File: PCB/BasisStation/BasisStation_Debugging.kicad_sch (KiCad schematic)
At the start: 14 parts, among them J1 USB_B_Micro, U1 D3V3XA4B10LP, U2 TLV75801PDRV, U3 CP2102N-Axx-xQFN28

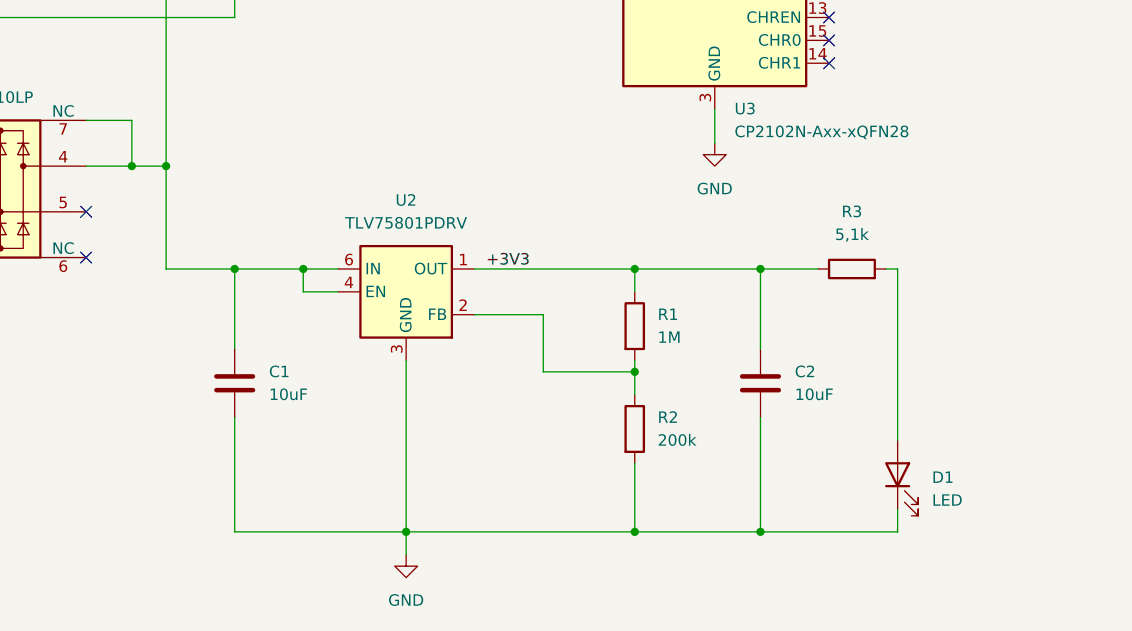
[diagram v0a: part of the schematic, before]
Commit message: Entfernung der LED im Debugging Layout
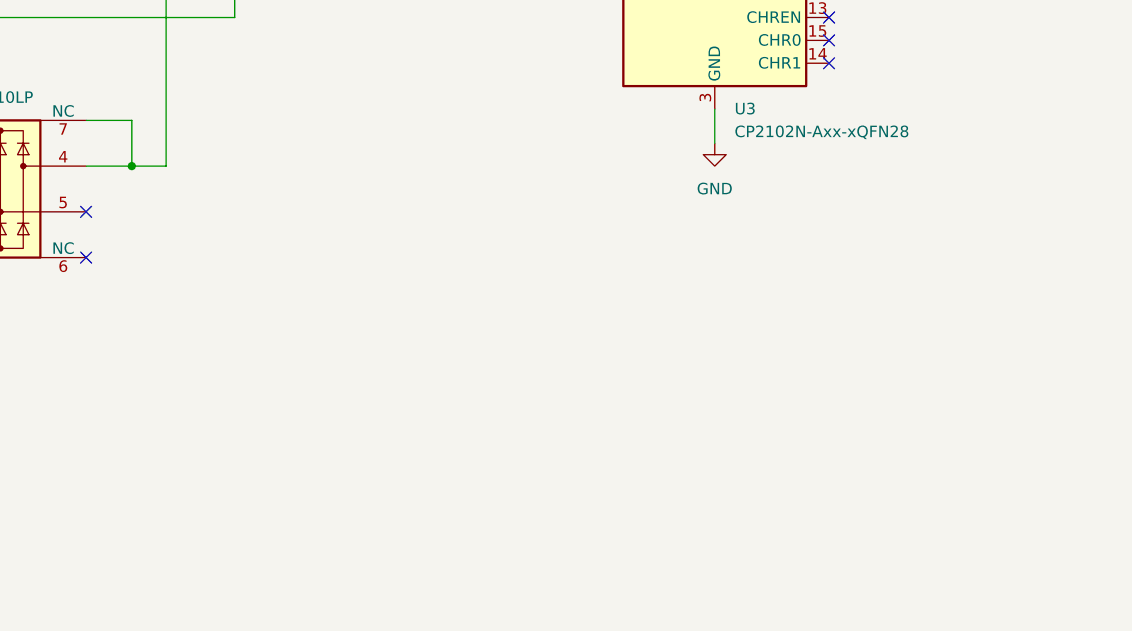
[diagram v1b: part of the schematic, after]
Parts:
- removed C1, C2: 10uF, symbol Device:C
- removed D1: LED, symbol Device:LED
- removed R1: 1M, symbol Device:R
- removed R2: 200k, symbol Device:R
- removed R3: 5,1k, symbol Device:R
- removed U2: TLV75801PDRV, Package_SON:WSON-6-1EP_2x2mm_P0.65mm_EP1x1.6mm, symbol Regulator_Linear:TLV75801PDRV

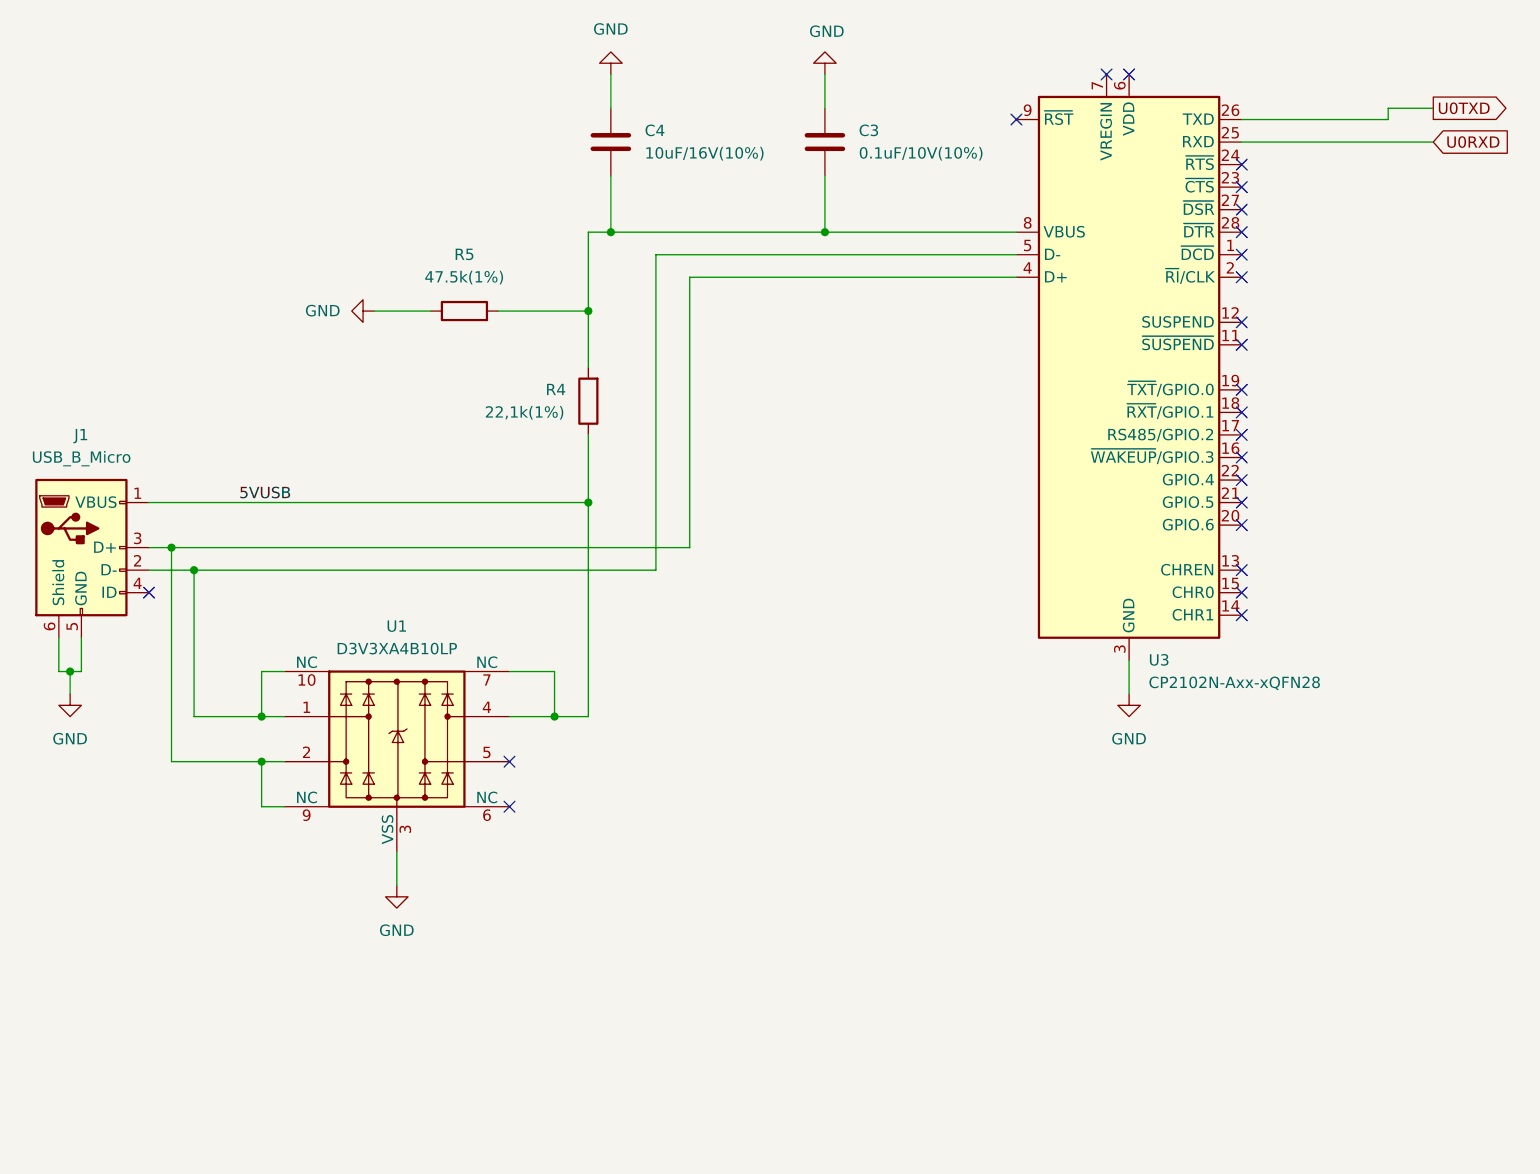
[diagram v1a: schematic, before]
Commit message: USB-Bridge entfernt. Globale Bezeichner USB+ und USB- hinzugefügt
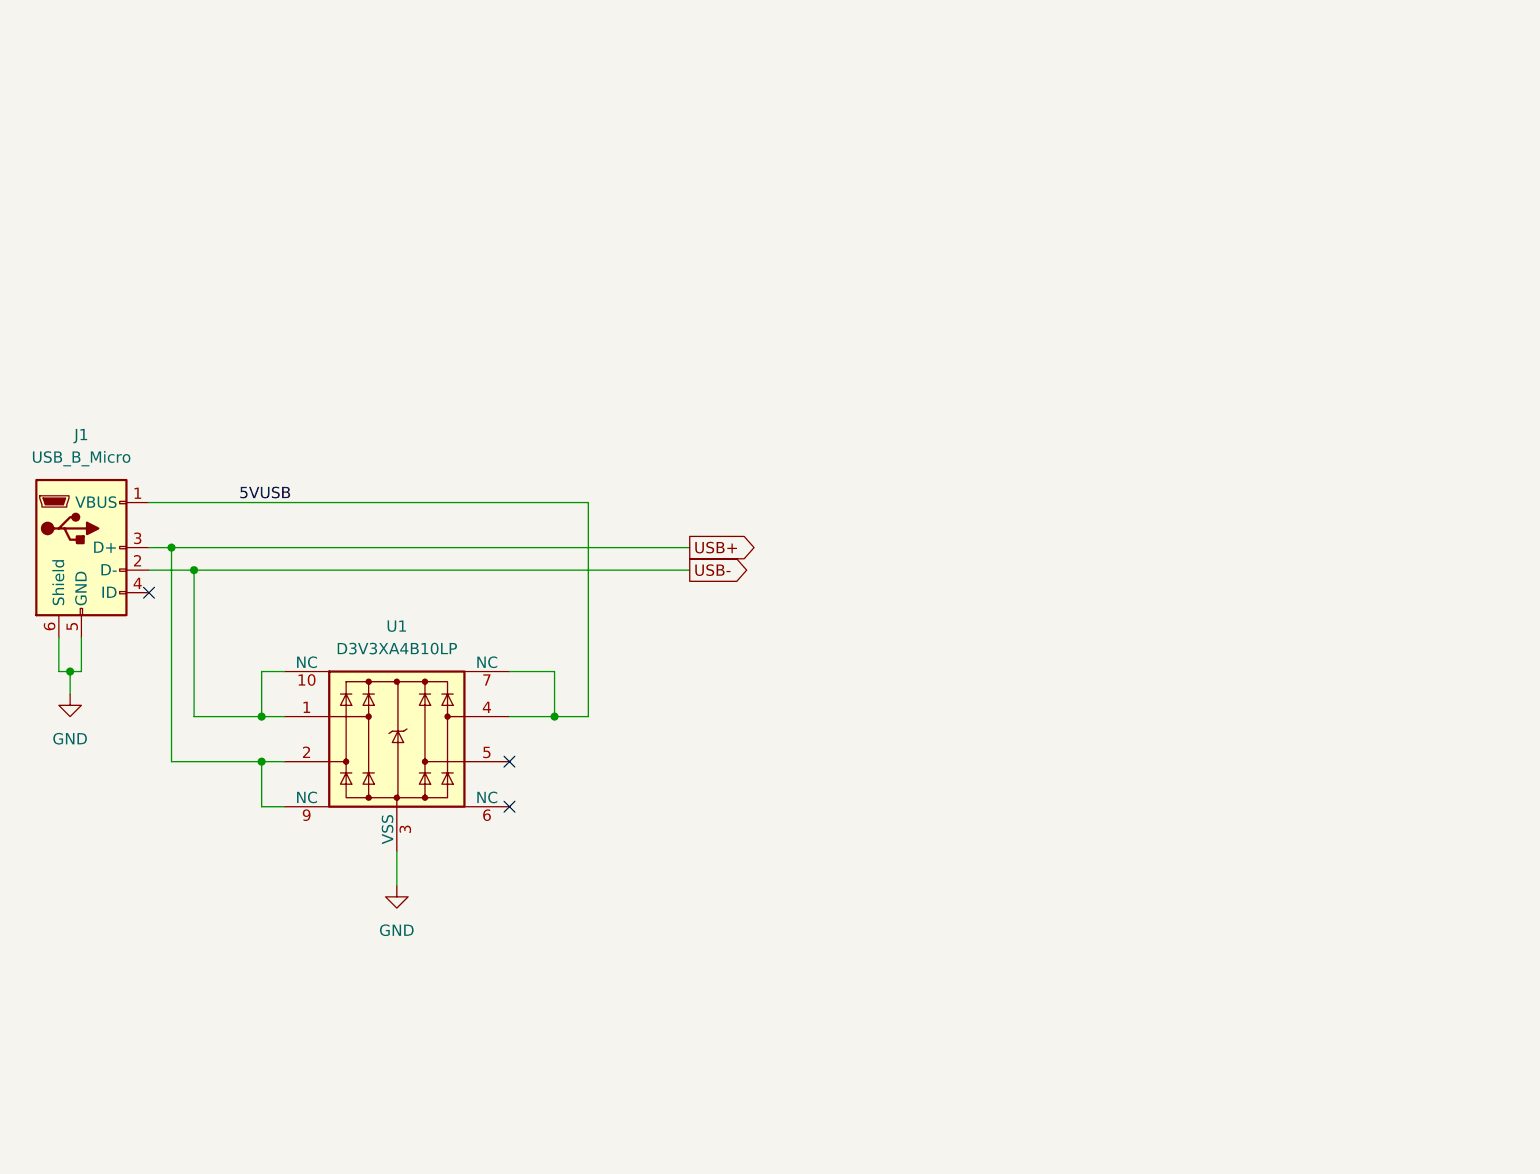
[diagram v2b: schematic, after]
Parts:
- removed C3: 0.1uF/10V(10%), symbol Device:C
- removed C4: 10uF/16V(10%), symbol Device:C
- removed R4: 22,1k(1%), symbol Device:R
- removed R5: 47.5k(1%), symbol Device:R
- removed U3: CP2102N-Axx-xQFN28, Package_DFN_QFN:QFN-28-1EP_5x5mm_P0.5mm_EP3.35x3.35mm, symbol Interface_USB:CP2102N-Axx-xQFN28
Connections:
- net USB-: now reaches J1.2 (D-), U1.1, U1.10 (NC)
- net USB+: now reaches J1.3 (D+), U1.2, U1.9 (NC)
- no-connect marks 24 -> 3
